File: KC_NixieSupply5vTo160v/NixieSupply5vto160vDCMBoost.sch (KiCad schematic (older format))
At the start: 47 parts, among them J1 Screw_Terminal_1x04, J2 CONN_01X01, J3 CONN_01X01, J4 CONN_01X01, J5 CONN_01X01, P1 USB_OTG, Q1 FDS2734CT, Q26 MMBTA42, U1 UCC3803

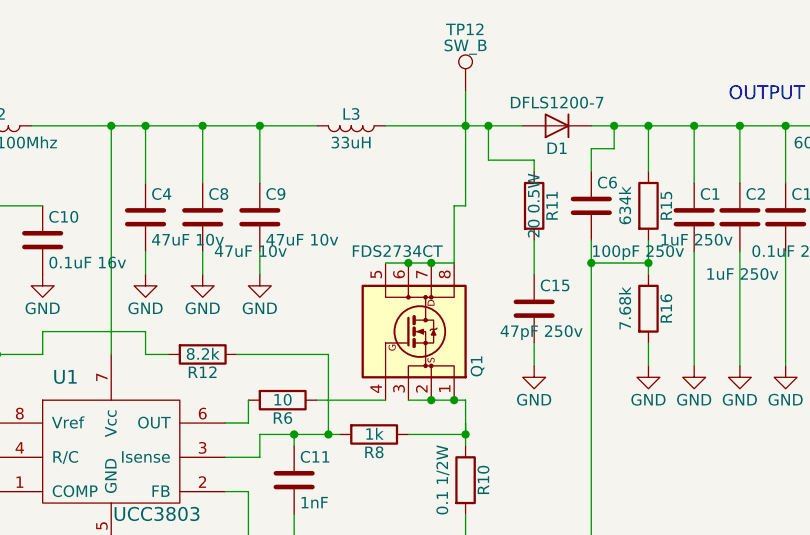
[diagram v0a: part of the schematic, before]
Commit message: New Gerber Files
Updated the layout of the USB connector to remove the Slots and replace
with holes.
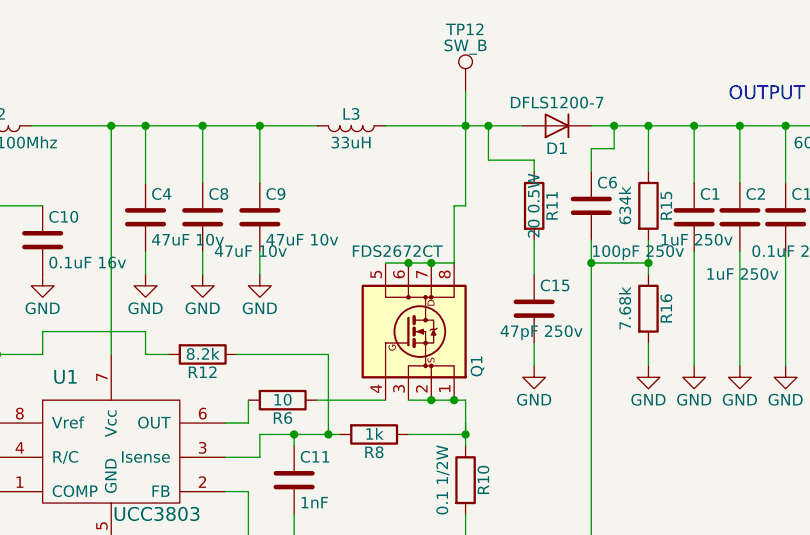
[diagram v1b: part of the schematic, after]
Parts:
- P1: footprint NixieSupply5vto160vDCMBoost_socket:USB_Micro-B_Wurth_3A -> NixieSupply5vto160vDCMBoost_socket:USB_Micro-B_Wurth_3A_Non-OVAL-Drill
- Q1: value FDS2734CT -> FDS2672CT
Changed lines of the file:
@@
 P 5900 2950
 F 0 "Q1" H 5700 3250 50  0000 L CNN
-F 1 "FDS2734CT" V 6250 2700 50  0000 L CNN
+F 1 "FDS2672CT" V 6250 2700 50  0000 L CNN
 F 2 "etaclock:SOIC-8-N" H 5900 2606 50  0001 C CIN
 F 3 "https://www.digikey.com/product-detail/en/on-semiconductor/FDS2672/FDS2672CT-ND/1217902" V 5900 2950 50  0001 L CNN
@@
 F 0 "P1" H 1925 2375 50  0000 C CNN
 F 1 "USB_OTG" H 1600 2850 50  0000 C CNN
-F 2 "NixieSupply5vto160vDCMBoost_socket:USB_Micro-B_Wurth_3A" V 1550 2400 50  0001 C CNN
+F 2 "NixieSupply5vto160vDCMBoost_socket:USB_Micro-B_Wurth_3A_Non-OVAL-Drill" V 1550 2400 50  0001 C CNN
 F 3 "https://www.digikey.com/product-detail/en/wurth-electronics-inc/629105150521/732-5960-1-ND/5047555" V 1550 2400 50  0001 C CNN
 F 4 "629105150521" H 1600 2500 60  0001 C CNN "MPN"
